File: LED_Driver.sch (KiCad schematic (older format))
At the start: 0 parts

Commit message: Added LED Block
Added LED Block Diagram (version 1)
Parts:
- added C? (x2): 1uF, ~, symbol C
- added D?: DIODESCH, ~, symbol DIODESCH
- added L?: 22uH, ~, symbol INDUCTOR
- added R?: 15, ~, symbol R
- added U?: APS726, symbol APS726
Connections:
- net String+: now also C?.1, D?.2 (K), U?.5 (OVP)
- net String-: now also R?.1, U?.3 (FB)
- new net: D?.1 (A), L?.2, U?.1 (SW)
- new net +5V: C?.1, L?.1, U?.6 (VIN)
- new net GND: C?.2, C?.2, R?.2, U?.2 (GND)
- new net LED_EN_PWM: U?.4 (EN)
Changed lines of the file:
@@
 $Descr A4 11693 8268
 encoding utf-8
-Sheet 6 9
+Sheet 9 9
 Title ""
-Date "23 sep 2013"
+Date "28 sep 2013"
 Rev ""
 Comp ""
@@
 Comment4 ""
 $EndDescr
-Text HLabel 1650 1600 0    60   Input ~ 0
-EN
-Text HLabel 1700 2050 0    60   Input ~ 0
-FREQ
-Text HLabel 9200 2950 0    60   Output ~ 0
+Text HLabel 1950 2900 0    60   Input ~ 0
+LED_EN_PWM
+Text HLabel 9350 1750 2    60   Output ~ 0
 String+
-Text HLabel 9200 3250 0    60   Input ~ 0
+Text HLabel 9350 2900 2    60   Input ~ 0
 String-
+$Comp
+L APS726 U?
+U 1 1 52466278
+P 3650 2750
+F 0 "U?" H 3950 2250 60  0000 C CNN
+F 1 "APS726" H 3650 2750 60  0000 C CNN
+F 2 "" H 3750 2650 60  0000 C CNN
+F 3 "" H 3750 2650 60  0000 C CNN
+	1    3650 2750
+	1    0    0    -1
+$EndComp
+$Comp
+L +5V #PWR?
+U 1 1 52466CD8
+P 3450 1450
+F 0 "#PWR?" H 3450 1540 20  0001 C CNN
+F 1 "+5V" H 3450 1540 30  0000 C CNN
+F 2 "" H 3450 1450 60  0000 C CNN
+F 3 "" H 3450 1450 60  0000 C CNN
+	1    3450 1450
+	1    0    0    -1
+$EndComp
+$Comp
+L GND #PWR?
+U 1 1 52466CE7
+P 3650 3850
+F 0 "#PWR?" H 3650 3850 30  0001 C CNN
+F 1 "GND" H 3650 3780 30  0001 C CNN
+F 2 "" H 3650 3850 60  0000 C CNN
+F 3 "" H 3650 3850 60  0000 C CNN
+	1    3650 3850
+	1    0    0    -1
+$EndComp
+$Comp
+L INDUCTOR L?
+U 1 1 52466D0A
+P 3900 1750
+F 0 "L?" V 3850 1750 40  0000 C CNN
+F 1 "22uH" V 4000 1750 40  0000 C CNN
+F 2 "~" H 3900 1750 60  0000 C CNN
+F 3 "~" H 3900 1750 60  0000 C CNN
+	1    3900 1750
+	0    -1   -1   0
+$EndComp
+$Comp
+L DIODESCH D?
+U 1 1 52466D38
+P 4600 1750
+F 0 "D?" H 4600 1850 40  0000 C CNN
+F 1 "DIODESCH" H 4600 1650 40  0000 C CNN
+F 2 "~" H 4600 1750 60  0000 C CNN
+F 3 "~" H 4600 1750 60  0000 C CNN
+	1    4600 1750
+	1    0    0    -1
+$EndComp
+$Comp
+L R R?
+U 1 1 52466D8B
+P 5100 3400
+F 0 "R?" V 5180 3400 40  0000 C CNN
+F 1 "15" V 5107 3401 40  0000 C CNN
+F 2 "~" V 5030 3400 30  0000 C CNN
+F 3 "~" H 5100 3400 30  0000 C CNN
+	1    5100 3400
+	1    0    0    -1
+$EndComp
+$Comp
+L C C?
+U 1 1 52466DC4
+P 9100 2200
+F 0 "C?" H 9100 2300 40  0000 L CNN
+F 1 "1uF" H 9106 2115 40  0000 L CNN
+F 2 "~" H 9138 2050 30  0000 C CNN
+F 3 "~" H 9100 2200 60  0000 C CNN
+	1    9100 2200
+	1    0    0    -1
+$EndComp
+$Comp
+L GND #PWR?
+U 1 1 52466DD1
+P 9100 2550
+F 0 "#PWR?" H 9100 2550 30  0001 C CNN
+F 1 "GND" H 9100 2480 30  0001 C CNN
+F 2 "" H 9100 2550 60  0000 C CNN
+F 3 "" H 9100 2550 60  0000 C CNN
+	1    9100 2550
+	1    0    0    -1
+$EndComp
+Wire Wire Line
+	1950 2900 3000 2900
+Wire Wire Line
+	3450 1450 3450 1650
+Wire Wire Line
+	3450 1650 3450 1750
+Wire Wire Line
+	3450 1750 3450 2100
+Wire Wire Line
+	3650 3450 3650 3700
+Wire Wire Line
+	3650 3700 3650 3850
+Wire Wire Line
+	3600 1750 3450 1750
+Connection ~ 3450 1750
+Wire Wire Line
+	4300 2900 5100 2900
+Wire Wire Line
+	5100 2900 9350 2900
+Wire Wire Line
+	5100 3150 5100 2900
+Connection ~ 5100 2900
+$Comp
+L C C?
+U 1 1 52466E2F
+P 3000 2000
+F 0 "C?" H 3000 2100 40  0000 L CNN
+F 1 "1uF" H 3006 1915 40  0000 L CNN
+F 2 "~" H 3038 1850 30  0000 C CNN
+F 3 "~" H 3000 2000 60  0000 C CNN
+	1    3000 2000
+	1    0    0    -1
+$EndComp
+$Comp
+L GND #PWR?
+U 1 1 52466E35
+P 3000 2400
+F 0 "#PWR?" H 3000 2400 30  0001 C CNN
+F 1 "GND" H 3000 2330 30  0001 C CNN
+F 2 "" H 3000 2400 60  0000 C CNN
+F 3 "" H 3000 2400 60  0000 C CNN
+	1    3000 2400
+	1    0    0    -1
+$EndComp
+Wire Wire Line
+	3000 2200 3000 2400
+Wire Wire Line
+	3450 1650 3000 1650
+Wire Wire Line
+	3000 1650 3000 1800
+Connection ~ 3450 1650
+Wire Wire Line
+	9100 2400 9100 2550
+Wire Wire Line
+	5100 3650 5100 3700
+Wire Wire Line
+	5100 3700 3650 3700
+Connection ~ 3650 3700
+Wire Wire Line
+	4200 1750 4300 1750
+Wire Wire Line
+	4300 1750 4400 1750
+Wire Wire Line
+	3850 2100 4300 2100
+Wire Wire Line
+	4300 2100 4300 1750
+Connection ~ 4300 1750
+Wire Wire Line
+	4800 1750 5000 1750
+Wire Wire Line
+	5000 1750 9100 1750
+Wire Wire Line
+	9100 1750 9350 1750
+Wire Wire Line
+	9100 2000 9100 1750
+Connection ~ 9100 1750
+Wire Wire Line
+	4300 2650 5000 2650
+Wire Wire Line
+	5000 2650 5000 1750
+Connection ~ 5000 1750
 $EndSCHEMATC

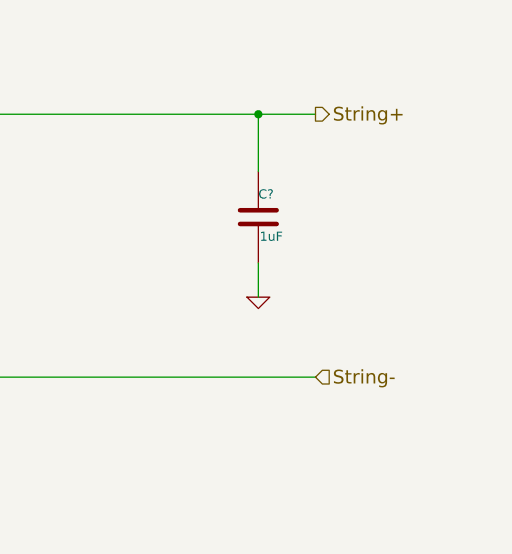
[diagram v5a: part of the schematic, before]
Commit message: Added Arduino Block
Added Arduino Block and connected the top level of the schematic.
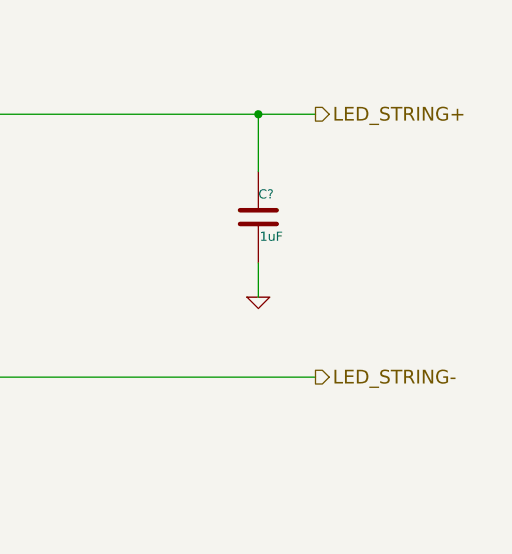
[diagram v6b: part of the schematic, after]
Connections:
- net String+ renamed LED_STRING+
- net String- renamed LED_STRING-
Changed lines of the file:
@@
 LED_EN_PWM
 Text HLabel 9350 1750 2    60   Output ~ 0
-String+
-Text HLabel 9350 2900 2    60   Input ~ 0
-String-
+LED_STRING+
+Text HLabel 9350 2900 2    60   Output ~ 0
+LED_STRING-
 $Comp
 L APS726 U?
